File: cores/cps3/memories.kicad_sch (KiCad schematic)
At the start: 12 parts

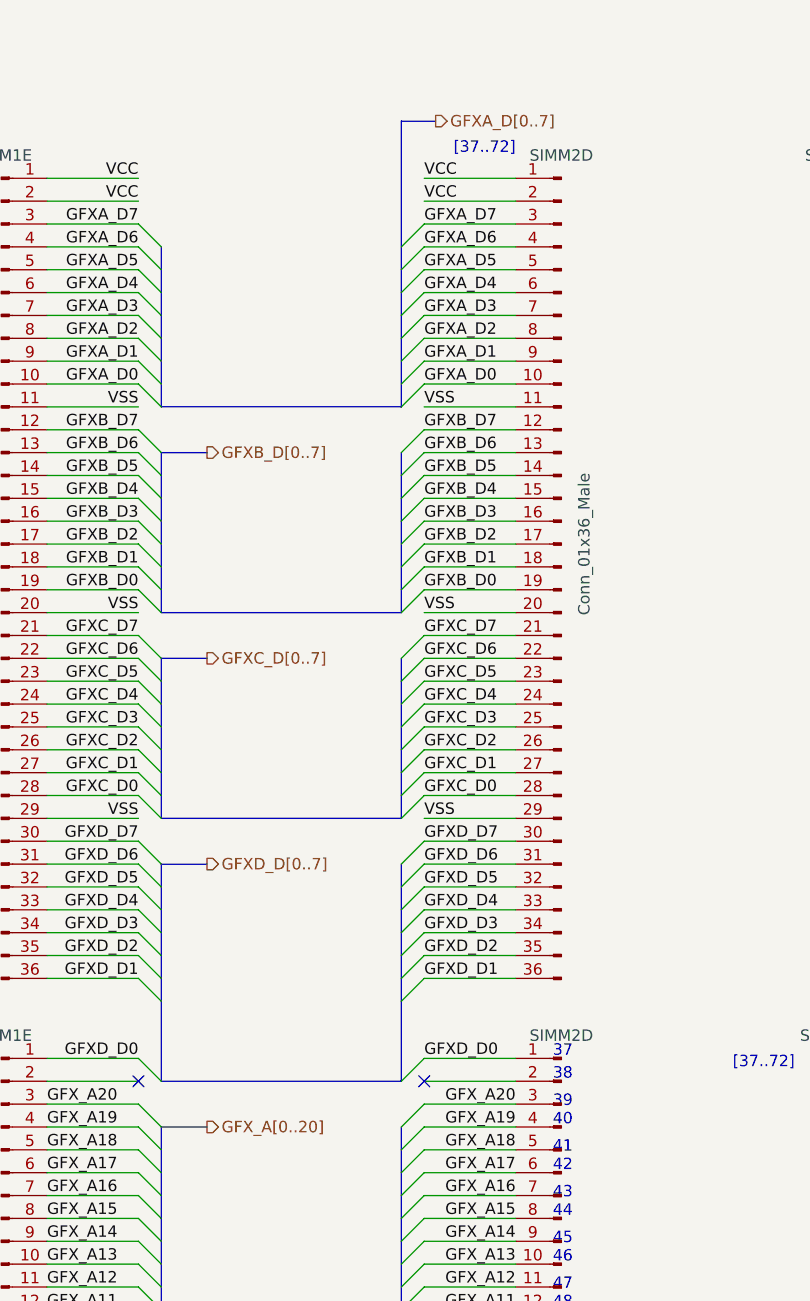
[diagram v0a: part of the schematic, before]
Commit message: moved sch folder
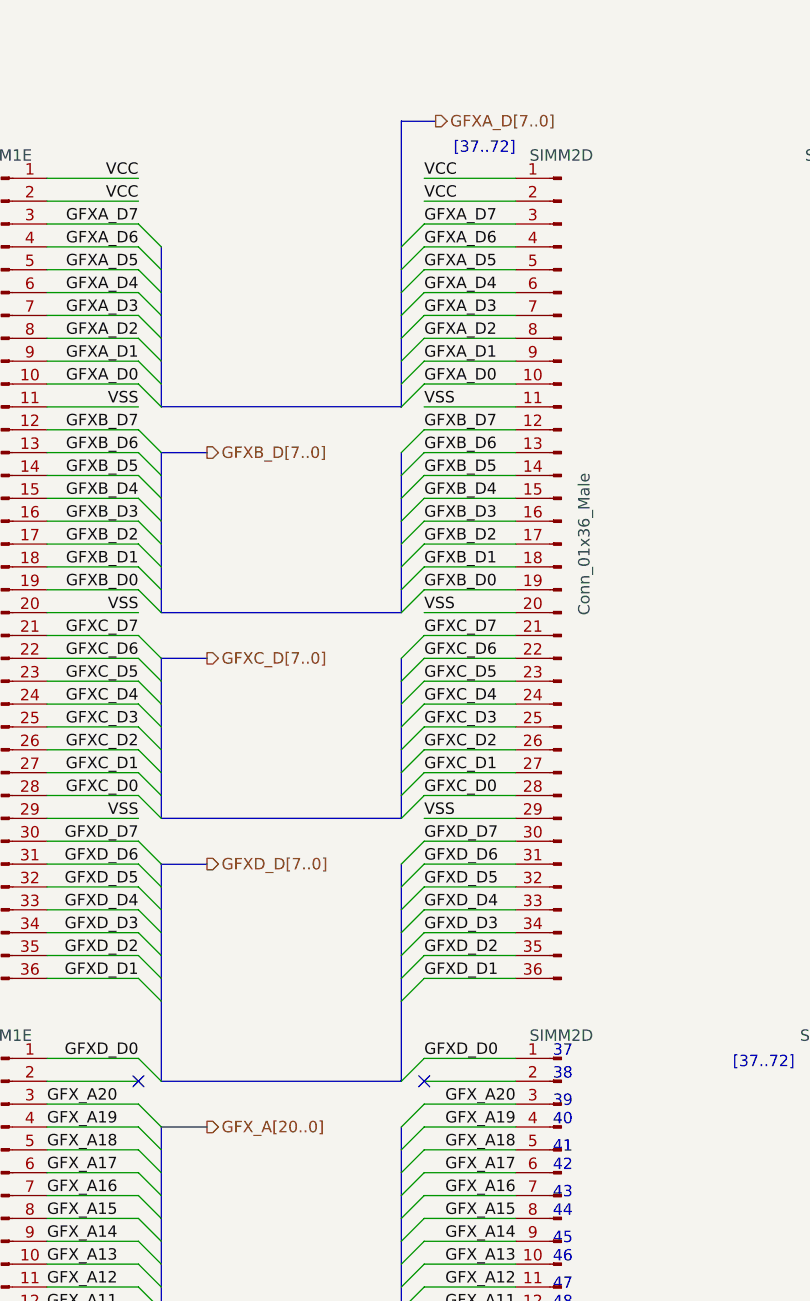
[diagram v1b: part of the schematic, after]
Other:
- company: (none) -> JOTEGO
- title: (none) -> CP SYSTEM III
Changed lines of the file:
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@@
   (paper "A3")
   (title_block
+    (title "CP SYSTEM III")
     (date "14/10/22")
+    (rev "José Tejada G.")
+    (company "JOTEGO")
+    (comment 1 "E.Triana")
   )
   (junction (at 295.91 232.41) (diameter 0) (color 0 0 0 0)
@@
     (effects (font (size 1.27 1.27)) (justify right))
   )
-  (hierarchical_label "GFXB_D[0..7]" (shape output) (at 167.64 71.12 0)
+  (hierarchical_label "GFXB_D[7..0]" (shape output) (at 167.64 71.12 0)
     (effects (font (size 1.27 1.27)) (justify left))
   )
@@
     (effects (font (size 1.27 1.27)) (justify right))
   )
-  (hierarchical_label "GFXC_D[0..7]" (shape output) (at 167.64 93.98 0)
+  (hierarchical_label "GFXC_D[7..0]" (shape output) (at 167.64 93.98 0)
     (effects (font (size 1.27 1.27)) (justify left))
   )
@@
     (effects (font (size 1.27 1.27)) (justify right))
   )
-  (hierarchical_label "GFXD_D[0..7]" (shape output) (at 167.64 116.84 0)
+  (hierarchical_label "GFXD_D[7..0]" (shape output) (at 167.64 116.84 0)
     (effects (font (size 1.27 1.27)) (justify left))
   )
@@
     (effects (font (size 1.27 1.27)) (justify left))
   )
-  (hierarchical_label "GFX_A[0..20]" (shape output) (at 167.64 146.05 0)
+  (hierarchical_label "GFX_A[20..0]" (shape output) (at 167.64 146.05 0)
     (effects (font (size 1.27 1.27)) (justify left))
   )
@@
     (effects (font (size 1.27 1.27)) (justify right))
   )
-  (hierarchical_label "GFXA_D[0..7]" (shape output) (at 193.04 34.29 0)
+  (hierarchical_label "GFXA_D[7..0]" (shape output) (at 193.04 34.29 0)
     (effects (font (size 1.27 1.27)) (justify left))
   )
